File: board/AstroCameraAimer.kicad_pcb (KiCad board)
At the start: 4 copper layers, 54.9 x 41.4 mm, 45 parts, among them J1 SBW, J2 Shutter Control, J3 LCD, J4 Battery, J5 Stepper Motor, Q1 PZT2222A, Q2 PZT2222A, SW1 SELECT, SW2 OK, U1 MSP430FR2433, U2 LM317, U3 A3967

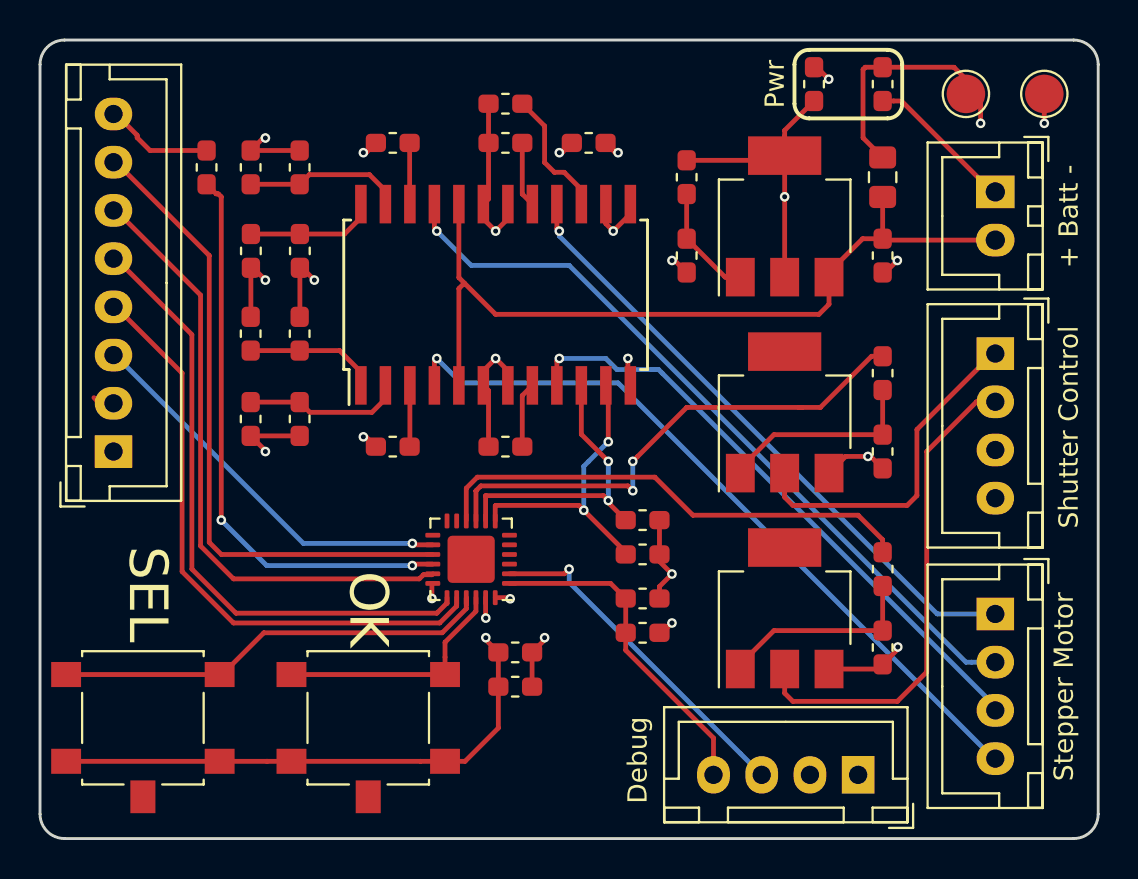
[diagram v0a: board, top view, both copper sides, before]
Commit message: Updated schematic and PCB to revision 3
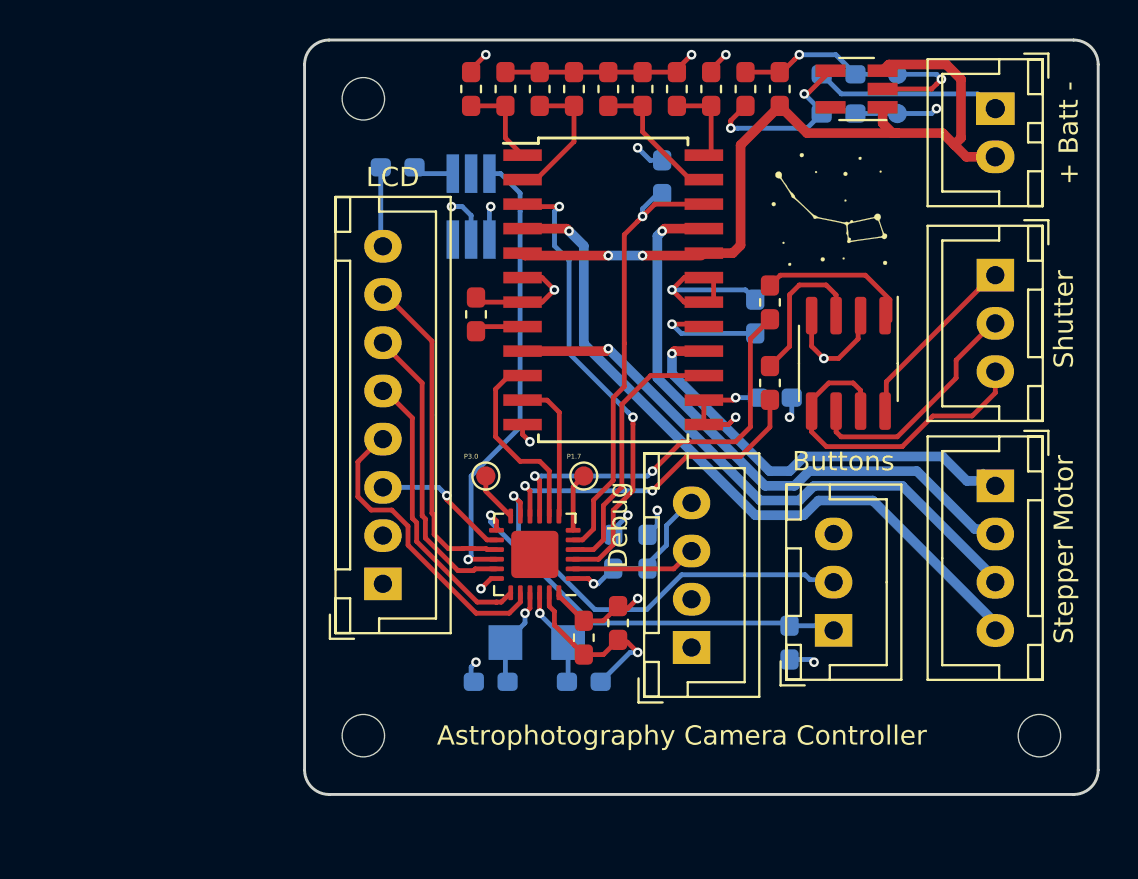
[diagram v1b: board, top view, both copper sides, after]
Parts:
- removed C5: 47uF, Capacitor_SMD:C_0805_2012Metric_Pad1.15x1.40mm_HandSolder
- removed C6: 0.1uF, Capacitor_SMD:C_0603_1608Metric_Pad1.05x0.95mm_HandSolder
- removed Q1, Q2: PZT2222A, Package_TO_SOT_SMD:SOT-223
- removed R13: 0.75, Resistor_SMD:R_0603_1608Metric_Pad1.05x0.95mm_HandSolder
- removed R14: 240, Resistor_SMD:R_0603_1608Metric_Pad1.05x0.95mm_HandSolder
- removed R18: 10K, Resistor_SMD:R_0603_1608Metric_Pad1.05x0.95mm_HandSolder
- removed R21, R22: JUMPER, Resistor_SMD:R_0603_1608Metric_Pad1.05x0.95mm_HandSolder
- removed R23: 390, Resistor_SMD:R_0603_1608Metric_Pad1.05x0.95mm_HandSolder
- removed R7: 13K, Resistor_SMD:R_0603_1608Metric_Pad1.05x0.95mm_HandSolder
- removed SW1: SELECT, Button_Switch_SMD:SW_SPST_B3S-1100
- removed SW2: OK, Button_Switch_SMD:SW_SPST_B3S-1100
- added C10: CL2, Capacitor_SMD:C_0603_1608Metric_Pad1.05x0.95mm_HandSolder, B.Cu at (141.2, 103.6)
- added C11: 1uF, Capacitor_SMD:C_0603_1608Metric_Pad1.05x0.95mm_HandSolder, F.Cu at (156.2, 72.9)
- added C12: 1uF, Capacitor_SMD:C_0603_1608Metric_Pad1.05x0.95mm_HandSolder, F.Cu at (154.4, 72.9)
- added C9: CL1, Capacitor_SMD:C_0603_1608Metric_Pad1.05x0.95mm_HandSolder, B.Cu at (146.1, 103.6)
- added H1: M2, MountingHole:MountingHole_2.2mm_M2, F.Cu at (134.6, 73.4)
- added H2: M2, MountingHole:MountingHole_2.2mm_M2, F.Cu at (134.6, 106.4)
- added H3: M2, MountingHole:MountingHole_2.2mm_M2, F.Cu at (169.7, 106.4)
- added J6: Buttons, Connector_JST:JST_XH_B03B-XH-A_1x03_P2.50mm_Vertical, F.Cu at (159.0, 101.0)
- added LG1: ProjectLogo, Logo:ursa_minor, F.Cu at (158.8, 79.2)
- added TP3: P3.0, TestPoint:TestPoint_Pad_D1.0mm, F.Cu at (141.0, 93.0)
- added TP4: P1.7, TestPoint:TestPoint_Pad_D1.0mm, F.Cu at (146.1, 93.0)
- added U4: NCP718, Package_TO_SOT_SMD:SOT-23-5_HandSoldering, F.Cu at (160.2, 72.9)
- added U5: SiP32510, Package_TO_SOT_SMD:TSOT-23-6_HandSoldering, B.Cu at (140.2, 79.0)
- added Y1: 32Khz, Crystal:Crystal_SMD_MicroCrystal_CC7V-T1A-2Pin_3.2x1.5mm_HandSoldering, B.Cu at (143.6, 101.6)
- C1, C4, R1: moved to B.Cu
- J2: value Shutter Control -> Shutter; footprint Connector_JST:JST_XH_B04B-XH-A_1x04_P2.50mm_Vertical -> Connector_JST:JST_XH_B03B-XH-A_1x03_P2.50mm_Vertical
- R10: value 390 -> 100K
- R11: value 20K -> 68K
- R12: value 0.75 -> JUMPER; moved to B.Cu
- R16: value 10K -> 0.75Ω; moved to B.Cu
- R17: value 10K -> 0.75Ω
- R19: value 10K -> JUMPER; moved to B.Cu
- R2: value 10K -> 100K; moved to B.Cu
- R20: value 10K -> 20K
- R3: value 10K -> 390
- R4: value 1K -> 390
- R5: value 1K -> 390; moved to B.Cu
- R6: value 20K -> 100K; moved to B.Cu
- R8: value 10K -> 13K
- R9: value 6.8K -> 20K
- TP1: value TP_GND -> GND; footprint TestPoint:TestPoint_Pad_D2.0mm -> TestPoint:TestPoint_Pad_D1.0mm; moved to B.Cu
- TP2: value TP_33V -> 3.3V; footprint TestPoint:TestPoint_Pad_D2.0mm -> TestPoint:TestPoint_Pad_D1.0mm; moved to B.Cu
- U2: value LM317 -> ILD205; footprint Package_TO_SOT_SMD:SOT-223-3_TabPin2 -> Package_SO:SOIC-8_3.9x4.9mm_P1.27mm
- moved R5 35.4 mm to (136.4, 77.0), turned to 0 degrees
- moved R11 27.9 mm to (150.9, 72.9), turned to 90 degrees
- moved R19 23.2 mm to (159.3, 74.2), turned to 180 degrees
- moved R6 22.8 mm to (150.1, 77.5)
- moved C7 21.2 mm to (143.8, 72.9)
- moved R12 17.6 mm to (159.3, 72.1)
- moved R15 17.2 mm to (145.5, 72.9)
- moved C8 16.5 mm to (147.3, 72.9), turned to 270 degrees
- moved C4 16.4 mm to (156.0, 88.9)
- moved R9 15.6 mm to (142.0, 72.9)
- moved J3 15.6 mm to (135.6, 98.6)
- moved R17 15.1 mm to (140.5, 84.6), turned to 270 degrees
- moved R3 15.0 mm to (155.7, 84.0), turned to 270 degrees
- moved R2 14.8 mm to (156.7, 101.6)
- moved R8 12.2 mm to (140.2, 72.9), turned to 270 degrees
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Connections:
- net Net-(J3-Pad3) renamed /LCD_nCS
- net Net-(J3-Pad4) renamed /LCD_RST
- net Net-(J3-Pad5) renamed /LCD_DC
- net Net-(J3-Pad6) renamed /LCD_MOSI
- net Net-(J3-Pad7) renamed /LCD_CLK
- net Net-(J5-Pad1) renamed /9V_Coil1A
- net Net-(J5-Pad2) renamed /9V_Coil1B
- net Net-(J5-Pad3) renamed /9V_Coil2A
- net Net-(J5-Pad4) renamed /9V_Coil2B
- C4 pad 1: +3V3 -> GND
- C4 pad 2: GND -> +3V3
- C7 pad 1: Net-(C7-Pad1) -> GND
- C7 pad 2: GND -> Net-(C7-Pad2)
- C8 pad 1: Net-(C8-Pad1) -> GND
- C8 pad 2: GND -> Net-(C8-Pad2)
- J2 pad 3: GND -> Net-(J2-Pad3)
- J4 pad 2: +9V -> BATT_9V
- R10 pad 1: Net-(R10-Pad1) -> +3V3
- R10 pad 2: GND -> Net-(R10-Pad2)
- R11 pad 1: Net-(C7-Pad1) -> Net-(R10-Pad2)
- R12 pad 1: GND -> Net-(J4-Pad1)
- R12 pad 2: Net-(R12-Pad2) -> GND
- R15 pad 1: Net-(C8-Pad1) -> Net-(C7-Pad2)
- R16 pad 1: Net-(R16-Pad1) -> GND
- R16 pad 2: GND -> Net-(R16-Pad2)
- R17 pad 1: Net-(R17-Pad1) -> GND
- R17 pad 2: GND -> Net-(R17-Pad2)
- R19 pad 2: Net-(R19-Pad2) -> SUPPLY_3.3V
- R2 pad 1: Net-(Q1-Pad1) -> +3V3
- R2 pad 2: FOCUS -> OK_BTN
- R20 pad 1: GND -> Net-(C8-Pad2)
- R20 pad 2: Net-(R20-Pad2) -> GND
- R3 pad 1: Net-(Q2-Pad1) -> Net-(R3-Pad1)
- R3 pad 2: SHUTTER -> FOCUS
- R4 pad 1: GND -> Net-(R4-Pad1)
- R4 pad 2: Net-(Q1-Pad1) -> SHUTTER
- R5 pad 1: GND -> Net-(J3-Pad8)
- R5 pad 2: Net-(Q2-Pad1) -> Net-(R5-Pad2)
- R6 pad 1: GND -> +3V3
- R6 pad 2: Net-(R6-Pad2) -> DRIVER_nRESET
- R9 pad 1: Net-(R8-Pad2) -> GND
- R9 pad 2: GND -> Net-(R8-Pad2)
- U1 pad 11: Net-(U1-Pad11) -> SELECT_BTN
- U1 pad 13: Net-(U1-Pad13) -> OK_BTN
- U1 pad 16: Net-(R23-Pad1) -> LCD_LED
- U1 pad 21: SELECT_BTN -> Net-(C10-Pad1)
- U1 pad 22: OK_BTN -> Net-(C9-Pad1)
- U1 pad 3: Net-(U1-Pad3) -> DRIVER_nSLEEP
- U1 pad 4: Net-(U1-Pad4) -> DRIVER_nENABLE
- U1 pad 5: Net-(U1-Pad5) -> DRIVER_nRESET
- U1 pad 7: Net-(R17-Pad1) -> DRIVER_DIR
- U1 pad 8: Net-(R16-Pad1) -> DRIVER_STEP
- U2 pad 1: Net-(R10-Pad1) -> Net-(R3-Pad1)
- U2 pad 2: Net-(R14-Pad1) -> GND
- U2 pad 3: +9V -> Net-(R4-Pad1)
- U3 pad 1: Net-(R6-Pad2) -> Net-(R8-Pad2)
- U3 pad 10: Net-(R16-Pad1) -> DRIVER_STEP
- U3 pad 11: Net-(R17-Pad1) -> DRIVER_DIR
- U3 pad 15: Net-(R20-Pad2) -> DRIVER_nENABLE
- U3 pad 17: Net-(R12-Pad2) -> Net-(R16-Pad2)
- U3 pad 2: Net-(C7-Pad1) -> Net-(C7-Pad2)
- U3 pad 20: +9V -> BATT_9V
- U3 pad 22: Net-(R19-Pad2) -> DRIVER_nRESET
- U3 pad 23: Net-(C8-Pad1) -> Net-(C8-Pad2)
- U3 pad 24: Net-(R8-Pad2) -> Net-(R10-Pad2)
- U3 pad 3: Net-(R18-Pad2) -> DRIVER_nSLEEP
- U3 pad 5: +9V -> BATT_9V
- U3 pad 8: Net-(R13-Pad2) -> Net-(R17-Pad2)
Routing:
- net +9V: track 42.8 -> 0.00 mm
- net BATT_9V: track 0.00 -> 41.8 mm, vias 0 -> 2
- net Net-(R23-Pad1): track 29.8 -> 0.00 mm, vias 2 -> 0
- net DRIVER_nSLEEP: track 0.00 -> 24.1 mm, vias 0 -> 2
- net LCD_LED: track 0.00 -> 23.6 mm, vias 0 -> 1
- net DRIVER_nRESET: track 0.00 -> 23.5 mm, vias 0 -> 1
- net GND: track 85.9 -> 62.5 mm, vias 15 -> 12
- net /LCD_DC: track 32.5 -> 15.1 mm
- net Net-(J2-Pad3): track 0.00 -> 17.4 mm
- net /LCD_MOSI: track 32.2 -> 15.4 mm
- net /LCD_CLK: track 33.7 -> 17.2 mm
- net Net-(R14-Pad1): track 16.0 -> 0.00 mm, vias 1 -> 0
- net Net-(R16-Pad1): track 15.9 -> 0.00 mm, vias 2 -> 0
- net Net-(R17-Pad1): track 15.7 -> 0.00 mm, vias 2 -> 0
- net /LCD_RST: track 31.5 -> 15.8 mm
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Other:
- board size 54.9 x 41.4 mm -> 41.1 x 39.1 mm
- net class 9V added: clearance 0.2, trace_width 0.5, via_dia 0.5, via_drill 0.254
- board text added: "*"
- board text added: "2019"
- board text added: "3V3"
- board text added: "Astrophotography Camera Controller"
- board text added: "Buttons"
- board text added: "Gnd"
- board text added: "LCD"
- board text added: "P1.7"
- board text added: "P3.0"
- board text added: "Revision 3"
- board text added: "Shutter"
- board text removed: "Astrophotography Camera Mount Controller"
- board text removed: "OK"
- board text removed: "Pwr"
- board text removed: "Rev 2"
- board text removed: "SEL"
- board text removed: "Shutter Control"

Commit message: Fix NCP718 footprint and update board to revision 4
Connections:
- U4 pad 4: SUPPLY_3.3V -> Net-(U4-Pad4)
- U4 pad 5: Net-(U4-Pad5) -> SUPPLY_3.3V
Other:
- board text added: "Revision 4"
- board text removed: "Revision 3"
